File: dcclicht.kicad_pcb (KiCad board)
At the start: 2 copper layers, 80 x 80 mm, 107 parts, among them J101 Power IN, J102 Debug, J103 CAN, J201 L1, J202 L2, J301 USB_B_Micro, Q101 BC860, Q201 AO3400A, Q202 AO3400A, Q203 AO3400A, Q204 AO3400A, Q205 AO3400A, Q206 AO3400A, Q207 AO3400A, Q208 AO3400A, SW101 Term, SW102 Reset, SW103 User, U101 AMS1117-3.3, U102 EL817S1(C)(TU)-F, U103 EL817S1(C)(TU)-F, U104 STM32F103CBTx, U105 TJA1042T, U106 ATECC608B-MAVDA-S, U301 XC6206P332MR, U302 CH340N, U303 USBLC6-2SC6, Y101 8MHz, Y102 32k

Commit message: Add legalese
Signed-off-by: Benedikt Spranger <b.spranger@linutronix.de>
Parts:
- added G***: LOGO, eurovibes:LOGO, F.Cu at (122.1, 65.4)
- added REF**: OSHW-Logo2_7.3x6mm_Copper, Symbol:OSHW-Logo2_7.3x6mm_Copper, F.Cu at (114.0, 71.0)
- added REF**: WEEE-Logo_4.2x6mm_SilkScreen, Symbol:WEEE-Logo_4.2x6mm_SilkScreen, F.Cu at (124.0, 95.0)
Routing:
- net GND: vias 24 -> 50
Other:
- board text added: "DCC Licht 0.1"

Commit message: Describe PWM signals with names
Signed-off-by: Benedikt Spranger <b.spranger@linutronix.de>
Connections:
- net Net-(D201-A) renamed /PWM/PWM1-
- net Net-(D201-K) renamed /PWM/PWM1+
- net Net-(D202-A) renamed /PWM/PWM2-
- net Net-(D202-K) renamed /PWM/PWM2+
- net Net-(D203-A) renamed /PWM/PWM3-
- net Net-(D203-K) renamed /PWM/PWM3+
- net Net-(D204-A) renamed /PWM/PWM4-
- net Net-(D204-K) renamed /PWM/PWM4+
- net Net-(D205-A) renamed /PWM/PWM5-
- net Net-(D205-K) renamed /PWM/PWM5+
- net Net-(D206-A) renamed /PWM/PWM6-
- net Net-(D206-K) renamed /PWM/PWM6+
- net Net-(D207-A) renamed /PWM/PWM7-
- net Net-(D207-K) renamed /PWM/PWM7+
- net Net-(D208-A) renamed /PWM/PWM8-
- net Net-(D208-K) renamed /PWM/PWM8+

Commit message: Add signal names foe CAN high/low
Signed-off-by: Benedikt Spranger <b.spranger@linutronix.de>
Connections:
- net Net-(J103-Pin_1) renamed /CAN_L
- net Net-(J103-Pin_2) renamed /CAN_H
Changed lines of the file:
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@@
 	(net 38 "/SWCLK")
 	(net 39 "/SWDIO")
-	(net 40 "Net-(J103-Pin_2)")
-	(net 41 "Net-(J103-Pin_1)")
+	(net 40 "/CAN_H")
+	(net 41 "/CAN_L")
 	(net 42 "/PWM/PWM8-")
 	(net 43 "/PWM/PWM8+")
@@
 			(layers "*.Cu" "*.Mask")
 			(remove_unused_layers no)
-			(net 41 "Net-(J103-Pin_1)")
+			(net 41 "/CAN_L")
 			(pinfunction "B")
 			(pintype "passive")
@@
 			(layers "*.Cu" "*.Mask")
 			(remove_unused_layers no)
-			(net 40 "Net-(J103-Pin_2)")
+			(net 40 "/CAN_H")
 			(pinfunction "B")
 			(pintype "passive")
@@
 			(layers "F.Cu" "F.Paste" "F.Mask")
 			(roundrect_rratio 0.25)
-			(net 41 "Net-(J103-Pin_1)")
+			(net 41 "/CAN_L")
 			(pinfunction "CANL")
 			(pintype "bidirectional")
@@
 			(layers "F.Cu" "F.Paste" "F.Mask")
 			(roundrect_rratio 0.25)
-			(net 40 "Net-(J103-Pin_2)")
+			(net 40 "/CAN_H")
 			(pinfunction "CANH")
 			(pintype "bidirectional")
@@
 			(layers "*.Cu" "*.Mask")
 			(remove_unused_layers no)
-			(net 41 "Net-(J103-Pin_1)")
+			(net 41 "/CAN_L")
 			(pinfunction "Pin_1")
 			(pintype "passive")
@@
 			(layers "*.Cu" "*.Mask")
 			(remove_unused_layers no)
-			(net 41 "Net-(J103-Pin_1)")
+			(net 41 "/CAN_L")
 			(pinfunction "Pin_1")
 			(pintype "passive")
@@
 			(layers "*.Cu" "*.Mask")
 			(remove_unused_layers no)
-			(net 40 "Net-(J103-Pin_2)")
+			(net 40 "/CAN_H")
 			(pinfunction "Pin_2")
 			(pintype "passive")
@@
 			(layers "*.Cu" "*.Mask")
 			(remove_unused_layers no)
-			(net 40 "Net-(J103-Pin_2)")
+			(net 40 "/CAN_H")
 			(pinfunction "Pin_2")
 			(pintype "passive")

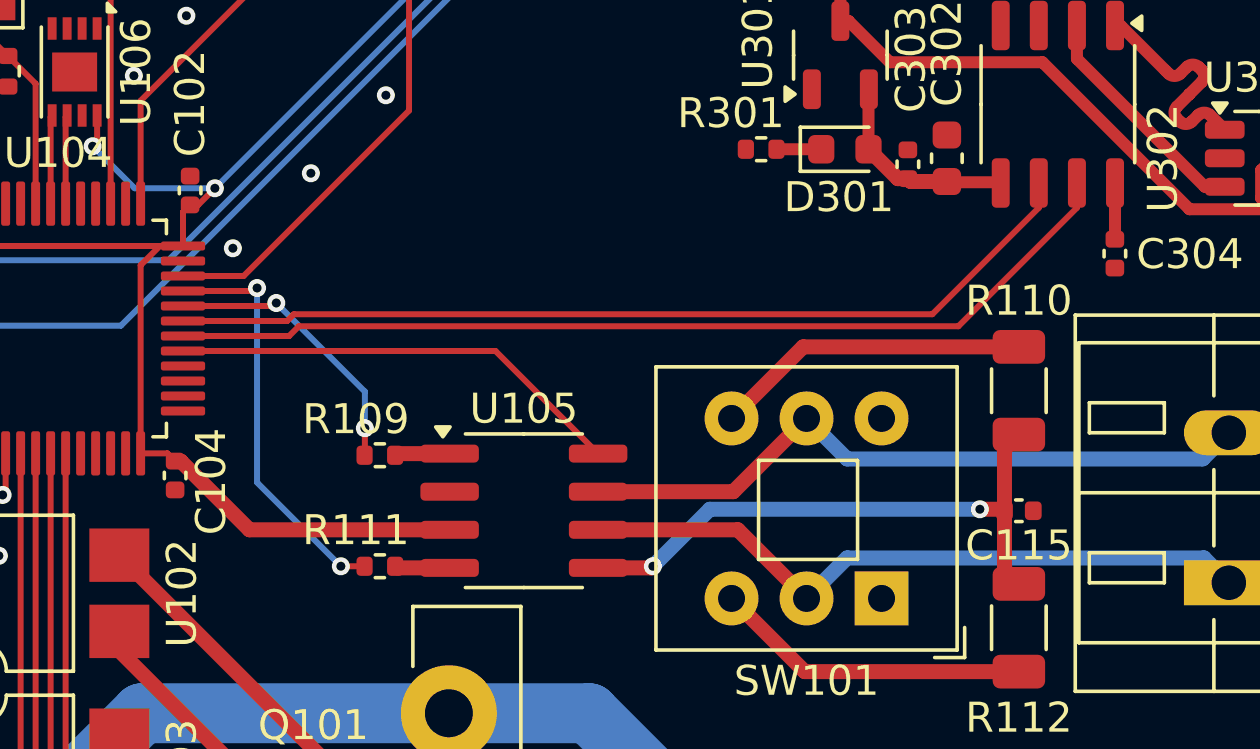
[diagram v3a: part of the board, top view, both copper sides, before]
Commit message: Switch CAN_RX and CAN_TX signals
Signed-off-by: Benedikt Spranger <b.spranger@linutronix.de>
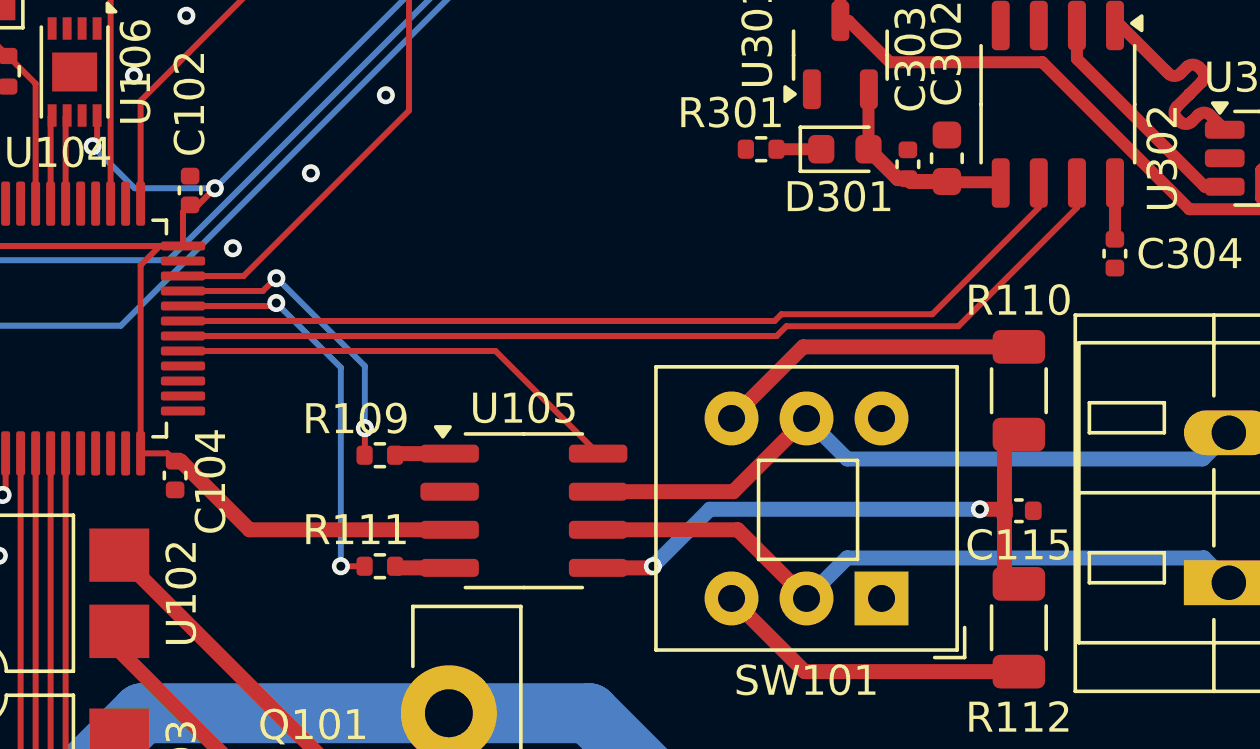
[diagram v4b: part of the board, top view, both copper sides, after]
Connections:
- U104 pad 32: /CAN_TX -> /CAN_RX
- U104 pad 33: /CAN_RX -> /CAN_TX
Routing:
- net /CAN_TX: track 9.45 -> 10.4 mm
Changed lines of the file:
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@@
 			(layers "F.Cu" "F.Paste" "F.Mask")
 			(roundrect_rratio 0.25)
-			(net 62 "/CAN_TX")
+			(net 64 "/CAN_RX")
 			(pinfunction "PA11")
 			(pintype "bidirectional")
@@
 			(layers "F.Cu" "F.Paste" "F.Mask")
 			(roundrect_rratio 0.25)
-			(net 64 "/CAN_RX")
+			(net 62 "/CAN_TX")
 			(pinfunction "PA12")
 			(pintype "bidirectional")
@@
 	)
 	(segment
-		(start 145.1375 81.425)
-		(end 148.146851 81.425)
+		(start 147.798322 80.925)
+		(end 148.223322 80.5)
 		(width 0.2)
 		(layer "F.Cu")
@@
 	)
 	(segment
+		(start 148.223322 80.5)
+		(end 148.25 80.5)
+		(width 0.2)
+		(layer "F.Cu")
+		(net 62)
+	)
+	(segment
 		(start 151.2 86.39)
 		(end 151.19 86.4)
@@
 	)
 	(segment
-		(start 148.146851 81.425)
-		(end 148.246851 81.325)
+		(start 145.1375 80.925)
+		(end 147.798322 80.925)
 		(width 0.2)
 		(layer "F.Cu")
@@
 	)
 	(via
-		(at 148.246851 81.325)
+		(at 148.25 80.5)
 		(size 0.6)
 		(drill 0.3)
@@
 	)
 	(segment
-		(start 151.2 85.5)
-		(end 151.2 84.278149)
+		(start 151.2 83.42962)
+		(end 151.2 85.5)
 		(width 0.2)
 		(layer "B.Cu")
@@
 	)
 	(segment
-		(start 151.2 84.278149)
-		(end 148.246851 81.325)
+		(start 148.25 80.5)
+		(end 148.27038 80.5)
+		(width 0.2)
+		(layer "B.Cu")
+		(net 62)
+	)
+	(segment
+		(start 148.27038 80.5)
+		(end 151.2 83.42962)
 		(width 0.2)
 		(layer "B.Cu")
@@
 	)
 	(segment
-		(start 150.4 90.1)
-		(end 151.19 90.1)
+		(start 145.1375 81.425)
+		(end 148.146851 81.425)
 		(width 0.2)
 		(layer "F.Cu")
@@
 	)
 	(segment
-		(start 147.506498 80.925)
-		(end 147.606498 80.825)
+		(start 150.4 90.1)
+		(end 151.19 90.1)
 		(width 0.2)
 		(layer "F.Cu")
@@
 	)
 	(segment
-		(start 145.1375 80.925)
-		(end 147.506498 80.925)
+		(start 148.146851 81.425)
+		(end 148.246851 81.325)
 		(width 0.2)
 		(layer "F.Cu")
@@
 	)
 	(via
-		(at 150.4 90.1)
+		(at 148.246851 81.325)
 		(size 0.6)
 		(drill 0.3)
@@
 	)
 	(via
-		(at 147.606498 80.825)
+		(at 150.4 90.1)
 		(size 0.6)
 		(drill 0.3)
@@
 	)
 	(segment
-		(start 147.606498 80.825)
-		(end 147.606498 87.306498)
+		(start 148.246851 81.325)
+		(end 150.4 83.478149)
 		(width 0.2)
 		(layer "B.Cu")
@@
 	)
 	(segment
-		(start 147.606498 87.306498)
+		(start 150.4 83.478149)
 		(end 150.4 90.1)
 		(width 0.2)
@@
 	)
 	(segment
-		(start 145.1375 82.425)
-		(end 148.675 82.425)
+		(start 174.935 78.149999)
+		(end 174.935 77.325)
 		(width 0.2)
 		(layer "F.Cu")
@@
 	)
 	(segment
-		(start 174.935 78.149999)
-		(end 170.984999 82.1)
+		(start 164.925 82.425)
+		(end 165.25 82.1)
 		(width 0.2)
 		(layer "F.Cu")
@@
 	(segment
 		(start 170.984999 82.1)
-		(end 149 82.1)
+		(end 174.935 78.149999)
 		(width 0.2)
 		(layer "F.Cu")
@@
 	)
 	(segment
-		(start 148.675 82.425)
-		(end 149 82.1)
+		(start 145.1375 82.425)
+		(end 164.925 82.425)
 		(width 0.2)
 		(layer "F.Cu")
@@
 	)
 	(segment
-		(start 174.935 77.325)
-		(end 174.935 78.149999)
+		(start 165.25 82.1)
+		(end 170.984999 82.1)
 		(width 0.2)
 		(layer "F.Cu")
@@
 	)
 	(segment
-		(start 148.834314 81.7)
-		(end 170.114999 81.7)
+		(start 145.1375 81.925)
+		(end 164.859314 81.925)
 		(width 0.2)
 		(layer "F.Cu")
@@
 	)
 	(segment
-		(start 148.609314 81.925)
-		(end 148.834314 81.7)
+		(start 170.114999 81.7)
+		(end 173.665 78.149999)
 		(width 0.2)
 		(layer "F.Cu")
@@
 	)
 	(segment
-		(start 173.665 78.149999)
-		(end 173.665 77.325)
+		(start 164.859314 81.925)
+		(end 165.084314 81.7)
 		(width 0.2)
 		(layer "F.Cu")
@@
 	)
 	(segment
-		(start 170.114999 81.7)
-		(end 173.665 78.149999)
+		(start 173.665 78.149999)
+		(end 173.665 77.325)
 		(width 0.2)
 		(layer "F.Cu")
@@
 	)
 	(segment
-		(start 145.1375 81.925)
-		(end 148.609314 81.925)
+		(start 165.084314 81.7)
+		(end 170.114999 81.7)
 		(width 0.2)
 		(layer "F.Cu")
